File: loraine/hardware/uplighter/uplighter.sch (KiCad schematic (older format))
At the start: 13 parts, among them K1 CONN_3, K2 CONN_3, K3 CONN_3, U1 TL4242, U2 TL4242, U3 TL4242

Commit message: Finished both PCBs apart from logos and checking
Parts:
- C1, C2, C3: value C -> 100n
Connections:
- net +5V renamed VCC
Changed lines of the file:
@@
 REF_RED
-$Comp
-L +5V #PWR07
-U 1 1 537A665B
-P 2650 1150
-F 0 "#PWR07" H 2650 1240 20  0001 C CNN
-F 1 "+5V" H 2650 1240 30  0000 C CNN
-F 2 "" H 2650 1150 60  0000 C CNN
-F 3 "" H 2650 1150 60  0000 C CNN
-	1    2650 1150
-	1    0    0    -1
-$EndComp
-$Comp
-L +5V #PWR08
-U 1 1 537A6711
-P 2650 3050
-F 0 "#PWR08" H 2650 3140 20  0001 C CNN
-F 1 "+5V" H 2650 3140 30  0000 C CNN
-F 2 "" H 2650 3050 60  0000 C CNN
-F 3 "" H 2650 3050 60  0000 C CNN
-	1    2650 3050
-	1    0    0    -1
-$EndComp
-$Comp
-L +5V #PWR09
-U 1 1 537A67B5
-P 2650 4950
-F 0 "#PWR09" H 2650 5040 20  0001 C CNN
-F 1 "+5V" H 2650 5040 30  0000 C CNN
-F 2 "" H 2650 4950 60  0000 C CNN
-F 3 "" H 2650 4950 60  0000 C CNN
-	1    2650 4950
-	1    0    0    -1
-$EndComp
-$Comp
-L +5V #PWR010
-U 1 1 537A6897
-P 6100 1650
-F 0 "#PWR010" H 6100 1740 20  0001 C CNN
-F 1 "+5V" H 6100 1740 30  0000 C CNN
-F 2 "" H 6100 1650 60  0000 C CNN
-F 3 "" H 6100 1650 60  0000 C CNN
-	1    6100 1650
-	1    0    0    -1
-$EndComp
 $Comp
 L C C1
@@
 P 5850 2000
 F 0 "C1" H 5850 2100 40  0000 L CNN
-F 1 "C" H 5856 1915 40  0000 L CNN
+F 1 "100n" H 5856 1915 40  0000 L CNN
 F 2 "" H 5888 1850 30  0000 C CNN
 F 3 "" H 5850 2000 60  0000 C CNN
@@
 P 6100 2000
 F 0 "C2" H 6100 2100 40  0000 L CNN
-F 1 "C" H 6106 1915 40  0000 L CNN
+F 1 "100n" H 6106 1915 40  0000 L CNN
 F 2 "" H 6138 1850 30  0000 C CNN
 F 3 "" H 6100 2000 60  0000 C CNN
@@
 P 6350 2000
 F 0 "C3" H 6350 2100 40  0000 L CNN
-F 1 "C" H 6356 1915 40  0000 L CNN
+F 1 "100n" H 6356 1915 40  0000 L CNN
 F 2 "" H 6388 1850 30  0000 C CNN
 F 3 "" H 6350 2000 60  0000 C CNN
@@
 	1    0    0    -1
 $EndComp
-Wire Wire Line
-	3150 1650 3450 1650
-Wire Wire Line
-	1950 1650 2300 1650
-Wire Wire Line
-	2200 2150 2750 2150
-Wire Wire Line
-	2200 1650 2200 2150
-Wire Wire Line
-	2300 1750 2100 1750
-Wire Wire Line
-	1950 1450 2300 1450
-Wire Wire Line
-	1950 1350 2050 1350
-Wire Wire Line
-	2050 1350 2050 1200
-Wire Wire Line
-	2050 1200 3250 1200
-Wire Wire Line
-	3250 1200 3250 1450
-Wire Wire Line
-	3250 1450 3150 1450
-Wire Wire Line
-	1950 1550 1950 1650
-Connection ~ 2200 1650
-Wire Wire Line
-	2100 1750 2100 2300
-Wire Wire Line
-	2100 2300 3450 2300
-Wire Wire Line
-	3150 3550 3450 3550
-Wire Wire Line
-	1950 3550 2300 3550
-Wire Wire Line
-	2200 4050 2750 4050
-Wire Wire Line
-	2200 3550 2200 4050
-Wire Wire Line
-	2300 3650 2100 3650
-Wire Wire Line
-	1950 3350 2300 3350
-Wire Wire Line
-	1950 3250 2050 3250
-Wire Wire Line
-	2050 3250 2050 3100
-Wire Wire Line
-	2050 3100 3250 3100
-Wire Wire Line
-	3250 3100 3250 3350
-Wire Wire Line
-	3250 3350 3150 3350
-Wire Wire Line
-	1950 3450 1950 3550
-Connection ~ 2200 3550
-Wire Wire Line
-	2100 3650 2100 4200
-Wire Wire Line
-	2100 4200 3450 4200
-Wire Wire Line
-	3150 5450 3450 5450
-Wire Wire Line
-	1950 5450 2300 5450
-Wire Wire Line
-	2200 5950 2750 5950
-Wire Wire Line
-	2200 5450 2200 5950
-Wire Wire Line
-	2300 5550 2100 5550
-Wire Wire Line
-	1950 5250 2300 5250
-Wire Wire Line
-	1950 5150 2050 5150
-Wire Wire Line
-	2050 5150 2050 5000
-Wire Wire Line
-	2050 5000 3250 5000
-Wire Wire Line
-	3250 5000 3250 5250
-Wire Wire Line
-	3250 5250 3150 5250
-Wire Wire Line
-	1950 5350 1950 5450
-Connection ~ 2200 5450
-Wire Wire Line
-	2100 5550 2100 6100
-Wire Wire Line
-	2100 6100 3450 6100
-Wire Wire Line
-	5700 4200 5700 5350
-Wire Wire Line
-	5900 4200 5900 5350
-Wire Wire Line
-	6100 4200 6100 5350
-Wire Wire Line
-	6100 5850 6100 5900
-Wire Wire Line
-	5900 5900 5900 5850
-Wire Wire Line
-	5700 5850 5700 5900
-Wire Wire Line
-	2500 2200 2500 2150
-Connection ~ 2500 2150
-Wire Wire Line
-	2500 4100 2500 4050
-Connection ~ 2500 4050
-Wire Wire Line
-	2500 6000 2500 5950
-Connection ~ 2500 5950
-Wire Wire Line
-	5150 3250 6100 3250
-Wire Wire Line
-	6100 3250 6100 3650
-Wire Wire Line
-	5150 3400 5900 3400
-Wire Wire Line
-	5900 3400 5900 3650
-Wire Wire Line
-	5150 3550 5700 3550
-Wire Wire Line
-	5700 3550 5700 3650
-Wire Wire Line
-	5100 4600 5700 4600
-Connection ~ 5700 4600
-Wire Wire Line
-	5100 4750 5900 4750
-Connection ~ 5900 4750
-Wire Wire Line
-	5100 4900 6100 4900
-Connection ~ 6100 4900
-Wire Wire Line
-	2650 1150 2650 1200
-Connection ~ 2650 1200
-Wire Wire Line
-	2650 3050 2650 3100
-Connection ~ 2650 3100
-Wire Wire Line
-	2650 4950 2650 5000
-Connection ~ 2650 5000
-Wire Wire Line
-	5850 1800 5850 1700
-Wire Wire Line
-	5850 1700 6350 1700
-Wire Wire Line
-	6350 1700 6350 1800
-Wire Wire Line
-	6100 1650 6100 1800
-Connection ~ 6100 1700
 $Comp
 L GND #PWR011
@@
 $EndComp
 Wire Wire Line
+	3150 1650 3450 1650
+Wire Wire Line
+	1950 1650 2300 1650
+Wire Wire Line
+	2200 2150 2750 2150
+Wire Wire Line
+	2200 1650 2200 2150
+Wire Wire Line
+	2300 1750 2100 1750
+Wire Wire Line
+	1950 1450 2300 1450
+Wire Wire Line
+	1950 1350 2050 1350
+Wire Wire Line
+	2050 1350 2050 1200
+Wire Wire Line
+	2050 1200 3250 1200
+Wire Wire Line
+	3250 1200 3250 1450
+Wire Wire Line
+	3250 1450 3150 1450
+Wire Wire Line
+	1950 1550 1950 1650
+Connection ~ 2200 1650
+Wire Wire Line
+	2100 1750 2100 2300
+Wire Wire Line
+	2100 2300 3450 2300
+Wire Wire Line
+	3150 3550 3450 3550
+Wire Wire Line
+	1950 3550 2300 3550
+Wire Wire Line
+	2200 4050 2750 4050
+Wire Wire Line
+	2200 3550 2200 4050
+Wire Wire Line
+	2300 3650 2100 3650
+Wire Wire Line
+	1950 3350 2300 3350
+Wire Wire Line
+	1950 3250 2050 3250
+Wire Wire Line
+	2050 3250 2050 3100
+Wire Wire Line
+	2050 3100 3250 3100
+Wire Wire Line
+	3250 3100 3250 3350
+Wire Wire Line
+	3250 3350 3150 3350
+Wire Wire Line
+	1950 3450 1950 3550
+Connection ~ 2200 3550
+Wire Wire Line
+	2100 3650 2100 4200
+Wire Wire Line
+	2100 4200 3450 4200
+Wire Wire Line
+	3150 5450 3450 5450
+Wire Wire Line
+	1950 5450 2300 5450
+Wire Wire Line
+	2200 5950 2750 5950
+Wire Wire Line
+	2200 5450 2200 5950
+Wire Wire Line
+	2300 5550 2100 5550
+Wire Wire Line
+	1950 5250 2300 5250
+Wire Wire Line
+	1950 5150 2050 5150
+Wire Wire Line
+	2050 5150 2050 5000
+Wire Wire Line
+	2050 5000 3250 5000
+Wire Wire Line
+	3250 5000 3250 5250
+Wire Wire Line
+	3250 5250 3150 5250
+Wire Wire Line
+	1950 5350 1950 5450
+Connection ~ 2200 5450
+Wire Wire Line
+	2100 5550 2100 6100
+Wire Wire Line
+	2100 6100 3450 6100
+Wire Wire Line
+	5700 4200 5700 5350
+Wire Wire Line
+	5900 4200 5900 5350
+Wire Wire Line
+	6100 4200 6100 5350
+Wire Wire Line
+	6100 5850 6100 5900
+Wire Wire Line
+	5900 5900 5900 5850
+Wire Wire Line
+	5700 5850 5700 5900
+Wire Wire Line
+	2500 2200 2500 2150
+Connection ~ 2500 2150
+Wire Wire Line
+	2500 4100 2500 4050
+Connection ~ 2500 4050
+Wire Wire Line
+	2500 6000 2500 5950
+Connection ~ 2500 5950
+Wire Wire Line
+	5150 3250 6100 3250
+Wire Wire Line
+	6100 3250 6100 3650
+Wire Wire Line
+	5150 3400 5900 3400
+Wire Wire Line
+	5900 3400 5900 3650
+Wire Wire Line
+	5150 3550 5700 3550
+Wire Wire Line
+	5700 3550 5700 3650
+Wire Wire Line
+	5100 4600 5700 4600
+Connection ~ 5700 4600
+Wire Wire Line
+	5100 4750 5900 4750
+Connection ~ 5900 4750
+Wire Wire Line
+	5100 4900 6100 4900
+Connection ~ 6100 4900
+Wire Wire Line
+	2650 1150 2650 1200
+Connection ~ 2650 1200
+Wire Wire Line
+	2650 3050 2650 3100
+Connection ~ 2650 3100
+Wire Wire Line
+	2650 4950 2650 5000
+Connection ~ 2650 5000
+Wire Wire Line
+	5850 1800 5850 1700
+Wire Wire Line
+	5850 1700 6350 1700
+Wire Wire Line
+	6350 1700 6350 1800
+Wire Wire Line
+	6100 1650 6100 1800
+Connection ~ 6100 1700
+Wire Wire Line
 	6100 2200 6100 2350
 Wire Wire Line
@@
 Wire Wire Line
 	6350 2300 6350 2200
+$Comp
+L VCC #PWR?
+U 1 1 53CC287B
+P 2650 1150
+F 0 "#PWR?" H 2650 1250 30  0001 C CNN
+F 1 "VCC" H 2650 1250 30  0000 C CNN
+F 2 "" H 2650 1150 60  0000 C CNN
+F 3 "" H 2650 1150 60  0000 C CNN
+	1    2650 1150
+	1    0    0    -1
+$EndComp
+$Comp
+L VCC #PWR?
+U 1 1 53CC28EB
+P 2650 3050
+F 0 "#PWR?" H 2650 3150 30  0001 C CNN
+F 1 "VCC" H 2650 3150 30  0000 C CNN
+F 2 "" H 2650 3050 60  0000 C CNN
+F 3 "" H 2650 3050 60  0000 C CNN
+	1    2650 3050
+	1    0    0    -1
+$EndComp
+$Comp
+L VCC #PWR?
+U 1 1 53CC2968
+P 2650 4950
+F 0 "#PWR?" H 2650 5050 30  0001 C CNN
+F 1 "VCC" H 2650 5050 30  0000 C CNN
+F 2 "" H 2650 4950 60  0000 C CNN
+F 3 "" H 2650 4950 60  0000 C CNN
+	1    2650 4950
+	1    0    0    -1
+$EndComp
+$Comp
+L VCC #PWR?
+U 1 1 53CC2A33
+P 6100 1650
+F 0 "#PWR?" H 6100 1750 30  0001 C CNN
+F 1 "VCC" H 6100 1750 30  0000 C CNN
+F 2 "" H 6100 1650 60  0000 C CNN
+F 3 "" H 6100 1650 60  0000 C CNN
+	1    6100 1650
+	1    0    0    -1
+$EndComp
 $EndSCHEMATC

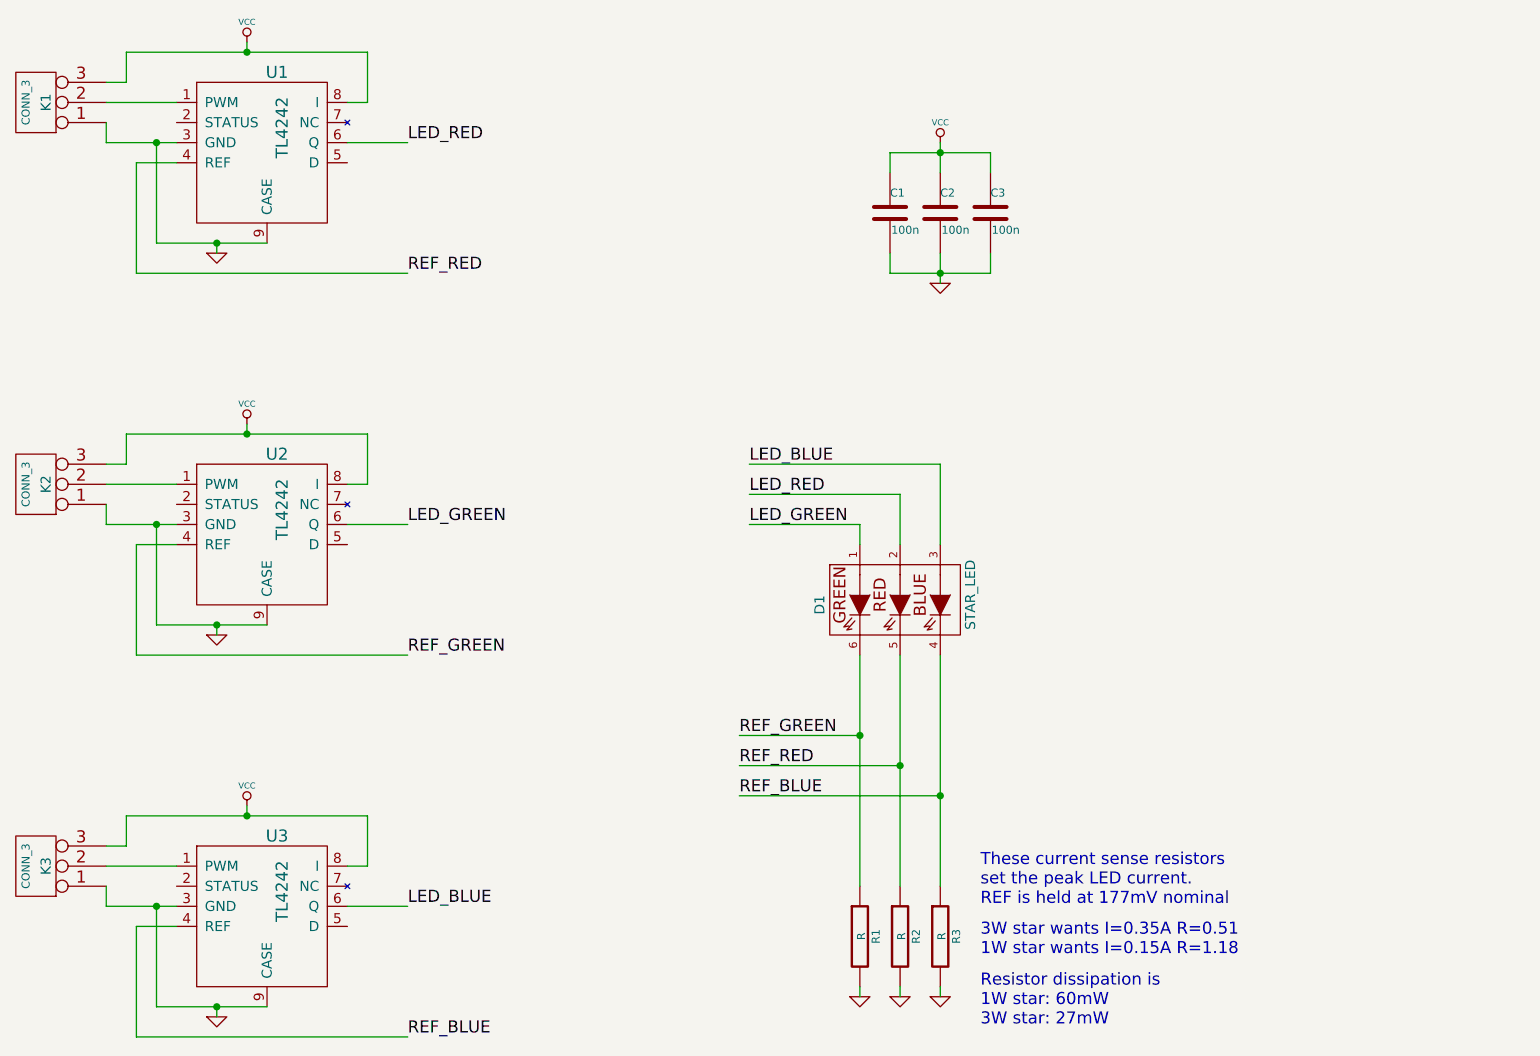
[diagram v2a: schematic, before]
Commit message: 5V power conn on uplighter board
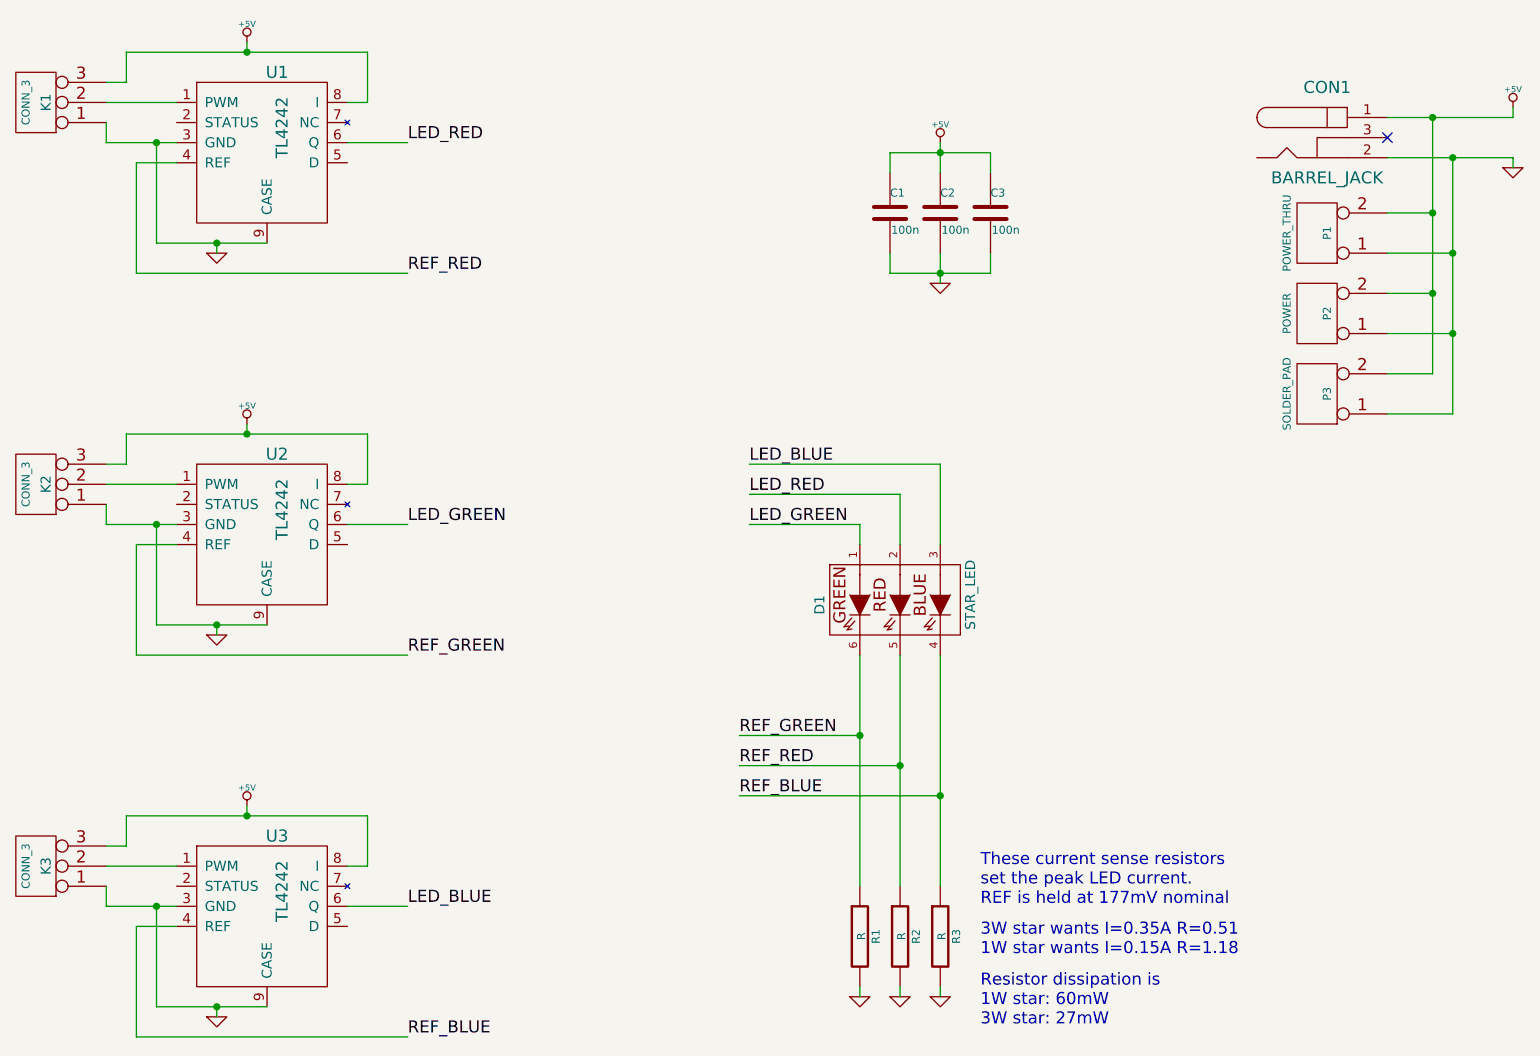
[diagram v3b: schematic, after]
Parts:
- added CON1: BARREL_JACK, symbol BARREL_JACK
- added P1: POWER_THRU, symbol CONN_2
- added P2: POWER, symbol CONN_2
- added P3: SOLDER_PAD, symbol CONN_2
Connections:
- net GND: now also CON1.2, P1.1 (P1), P2.1 (P1), P3.1 (P1)
- net VCC renamed +5V
- net +5V: now also CON1.1, P1.2 (PM), P2.2 (PM), P3.2 (PM)
- no-connect marks 0 -> 1
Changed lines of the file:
@@
 REF_BLUE
 $Comp
-L GND #PWR01
+L GND #PWR7
 U 1 1 53790258
 P 5700 5900
-F 0 "#PWR01" H 5700 5900 30  0001 C CNN
+F 0 "#PWR7" H 5700 5900 30  0001 C CNN
 F 1 "GND" H 5700 5830 30  0001 C CNN
 F 2 "" H 5700 5900 60  0000 C CNN
@@
 $EndComp
 $Comp
-L GND #PWR02
+L GND #PWR8
 U 1 1 53790276
 P 5900 5900
-F 0 "#PWR02" H 5900 5900 30  0001 C CNN
+F 0 "#PWR8" H 5900 5900 30  0001 C CNN
 F 1 "GND" H 5900 5830 30  0001 C CNN
 F 2 "" H 5900 5900 60  0000 C CNN
@@
 $EndComp
 $Comp
-L GND #PWR03
+L GND #PWR11
 U 1 1 53790294
 P 6100 5900
-F 0 "#PWR03" H 6100 5900 30  0001 C CNN
+F 0 "#PWR11" H 6100 5900 30  0001 C CNN
 F 1 "GND" H 6100 5830 30  0001 C CNN
 F 2 "" H 6100 5900 60  0000 C CNN
@@
 $EndComp
 $Comp
-L GND #PWR04
+L GND #PWR1
 U 1 1 537904E9
 P 2500 2200
-F 0 "#PWR04" H 2500 2200 30  0001 C CNN
+F 0 "#PWR1" H 2500 2200 30  0001 C CNN
 F 1 "GND" H 2500 2130 30  0001 C CNN
 F 2 "" H 2500 2200 60  0000 C CNN
@@
 $EndComp
 $Comp
-L GND #PWR05
+L GND #PWR2
 U 1 1 537905EA
 P 2500 4100
-F 0 "#PWR05" H 2500 4100 30  0001 C CNN
+F 0 "#PWR2" H 2500 4100 30  0001 C CNN
 F 1 "GND" H 2500 4030 30  0001 C CNN
 F 2 "" H 2500 4100 60  0000 C CNN
@@
 $EndComp
 $Comp
-L GND #PWR06
+L GND #PWR3
 U 1 1 53790784
 P 2500 6000
-F 0 "#PWR06" H 2500 6000 30  0001 C CNN
+F 0 "#PWR3" H 2500 6000 30  0001 C CNN
 F 1 "GND" H 2500 5930 30  0001 C CNN
 F 2 "" H 2500 6000 60  0000 C CNN
@@
 $EndComp
 $Comp
-L GND #PWR011
+L GND #PWR10
 U 1 1 537A6CCB
 P 6100 2350
-F 0 "#PWR011" H 6100 2350 30  0001 C CNN
+F 0 "#PWR10" H 6100 2350 30  0001 C CNN
 F 1 "GND" H 6100 2280 30  0001 C CNN
 F 2 "" H 6100 2350 60  0000 C CNN
@@
 	6350 2300 6350 2200
 $Comp
-L VCC #PWR?
-U 1 1 53CC287B
+L BARREL_JACK CON1
+U 1 1 53CD6288
+P 8025 1625
+F 0 "CON1" H 8025 1875 60  0000 C CNN
+F 1 "BARREL_JACK" H 8025 1425 60  0000 C CNN
+F 2 "" H 8025 1625 60  0000 C CNN
+F 3 "" H 8025 1625 60  0000 C CNN
+	1    8025 1625
+	1    0    0    -1
+$EndComp
+$Comp
+L CONN_2 P1
+U 1 1 53CD6307
+P 7975 2100
+F 0 "P1" V 7925 2100 40  0000 C CNN
+F 1 "POWER_THRU" V 8125 2100 40  0000 C CNN
+F 2 "" H 7975 2100 60  0000 C CNN
+F 3 "" H 7975 2100 60  0000 C CNN
+	1    7975 2100
+	-1   0    0    1
+$EndComp
+$Comp
+L CONN_2 P2
+U 1 1 53CD63AF
+P 7975 2500
+F 0 "P2" V 7925 2500 40  0000 C CNN
+F 1 "POWER" V 8125 2500 40  0000 C CNN
+F 2 "" H 7975 2500 60  0000 C CNN
+F 3 "" H 7975 2500 60  0000 C CNN
+	1    7975 2500
+	-1   0    0    1
+$EndComp
+$Comp
+L CONN_2 P3
+U 1 1 53CD640C
+P 7975 2900
+F 0 "P3" V 7925 2900 40  0000 C CNN
+F 1 "SOLDER_PAD" V 8125 2900 40  0000 C CNN
+F 2 "" H 7975 2900 60  0000 C CNN
+F 3 "" H 7975 2900 60  0000 C CNN
+	1    7975 2900
+	-1   0    0    1
+$EndComp
+Wire Wire Line
+	8325 1525 8950 1525
+Wire Wire Line
+	8550 1525 8550 2800
+Wire Wire Line
+	8550 2000 8325 2000
+Wire Wire Line
+	8550 2400 8325 2400
+Connection ~ 8550 2000
+Wire Wire Line
+	8550 2800 8325 2800
+Connection ~ 8550 2400
+NoConn ~ 8325 1625
+Wire Wire Line
+	8325 1725 8950 1725
+Wire Wire Line
+	8650 1725 8650 3000
+Wire Wire Line
+	8650 2200 8325 2200
+Wire Wire Line
+	8650 2600 8325 2600
+Connection ~ 8650 2200
+Wire Wire Line
+	8650 3000 8325 3000
+Connection ~ 8650 2600
+$Comp
+L +5V #PWR4
+U 1 1 53CD6A41
 P 2650 1150
-F 0 "#PWR?" H 2650 1250 30  0001 C CNN
-F 1 "VCC" H 2650 1250 30  0000 C CNN
+F 0 "#PWR4" H 2650 1240 20  0001 C CNN
+F 1 "+5V" H 2650 1240 30  0000 C CNN
 F 2 "" H 2650 1150 60  0000 C CNN
 F 3 "" H 2650 1150 60  0000 C CNN
@@
 $EndComp
 $Comp
-L VCC #PWR?
-U 1 1 53CC28EB
+L +5V #PWR5
+U 1 1 53CD6ACD
 P 2650 3050
-F 0 "#PWR?" H 2650 3150 30  0001 C CNN
-F 1 "VCC" H 2650 3150 30  0000 C CNN
+F 0 "#PWR5" H 2650 3140 20  0001 C CNN
+F 1 "+5V" H 2650 3140 30  0000 C CNN
 F 2 "" H 2650 3050 60  0000 C CNN
 F 3 "" H 2650 3050 60  0000 C CNN
@@
 $EndComp
 $Comp
-L VCC #PWR?
-U 1 1 53CC2968
+L +5V #PWR6
+U 1 1 53CD6B6A
 P 2650 4950
-F 0 "#PWR?" H 2650 5050 30  0001 C CNN
-F 1 "VCC" H 2650 5050 30  0000 C CNN
+F 0 "#PWR6" H 2650 5040 20  0001 C CNN
+F 1 "+5V" H 2650 5040 30  0000 C CNN
 F 2 "" H 2650 4950 60  0000 C CNN
 F 3 "" H 2650 4950 60  0000 C CNN
@@
 $EndComp
 $Comp
-L VCC #PWR?
-U 1 1 53CC2A33
+L +5V #PWR9
+U 1 1 53CD6C4B
 P 6100 1650
-F 0 "#PWR?" H 6100 1750 30  0001 C CNN
-F 1 "VCC" H 6100 1750 30  0000 C CNN
+F 0 "#PWR9" H 6100 1740 20  0001 C CNN
+F 1 "+5V" H 6100 1740 30  0000 C CNN
 F 2 "" H 6100 1650 60  0000 C CNN
 F 3 "" H 6100 1650 60  0000 C CNN
@@
 	1    0    0    -1
 $EndComp
+Connection ~ 8550 1525
+Wire Wire Line
+	8950 1525 8950 1475
+$Comp
+L +5V #PWR12
+U 1 1 53CD7008
+P 8950 1475
+F 0 "#PWR12" H 8950 1565 20  0001 C CNN
+F 1 "+5V" H 8950 1565 30  0000 C CNN
+F 2 "" H 8950 1475 60  0000 C CNN
+F 3 "" H 8950 1475 60  0000 C CNN
+	1    8950 1475
+	1    0    0    -1
+$EndComp
+Wire Wire Line
+	8950 1725 8950 1775
+Connection ~ 8650 1725
+$Comp
+L GND #PWR13
+U 1 1 53CD70A7
+P 8950 1775
+F 0 "#PWR13" H 8950 1775 30  0001 C CNN
+F 1 "GND" H 8950 1705 30  0001 C CNN
+F 2 "" H 8950 1775 60  0000 C CNN
+F 3 "" H 8950 1775 60  0000 C CNN
+	1    8950 1775
+	1    0    0    -1
+$EndComp
